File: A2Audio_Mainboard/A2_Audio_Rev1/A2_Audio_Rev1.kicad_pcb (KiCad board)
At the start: 4 copper layers, 30 parts, among them IC1 ES9822QPRO, U1 USBLC6-2SC6, U10 OPA1622IDRCR, U11 SI4732-A10-GS, U12 OPA1612AIDR, U13 LT3042xMSE, U14 W25Q16JVSS, U15 CM5108000, U16 AP2112K-3.3, U17 AP2112K-1.8, U18 LT6711A, U19 TPS62130, U2 TPS65987DDHRSHR, U20 AP2112K-1.8, U21 TPS61230DRC, U22 AP2112K-1.2, U23 LTC2954ITS8-1_TRPBF, U24 TPS65131RGE, U25 LT3094xDD, U26 TS5A3159DBVR, U3 TUSB546A-DCIRNQR, U4 BQ25895RTWR, U5 MAX17055ETB_T, U6 U_DAC_L, U7 U_DAC_R, U8 TPS7A2018PDBVR, U9 TPS7A2033PDBVR

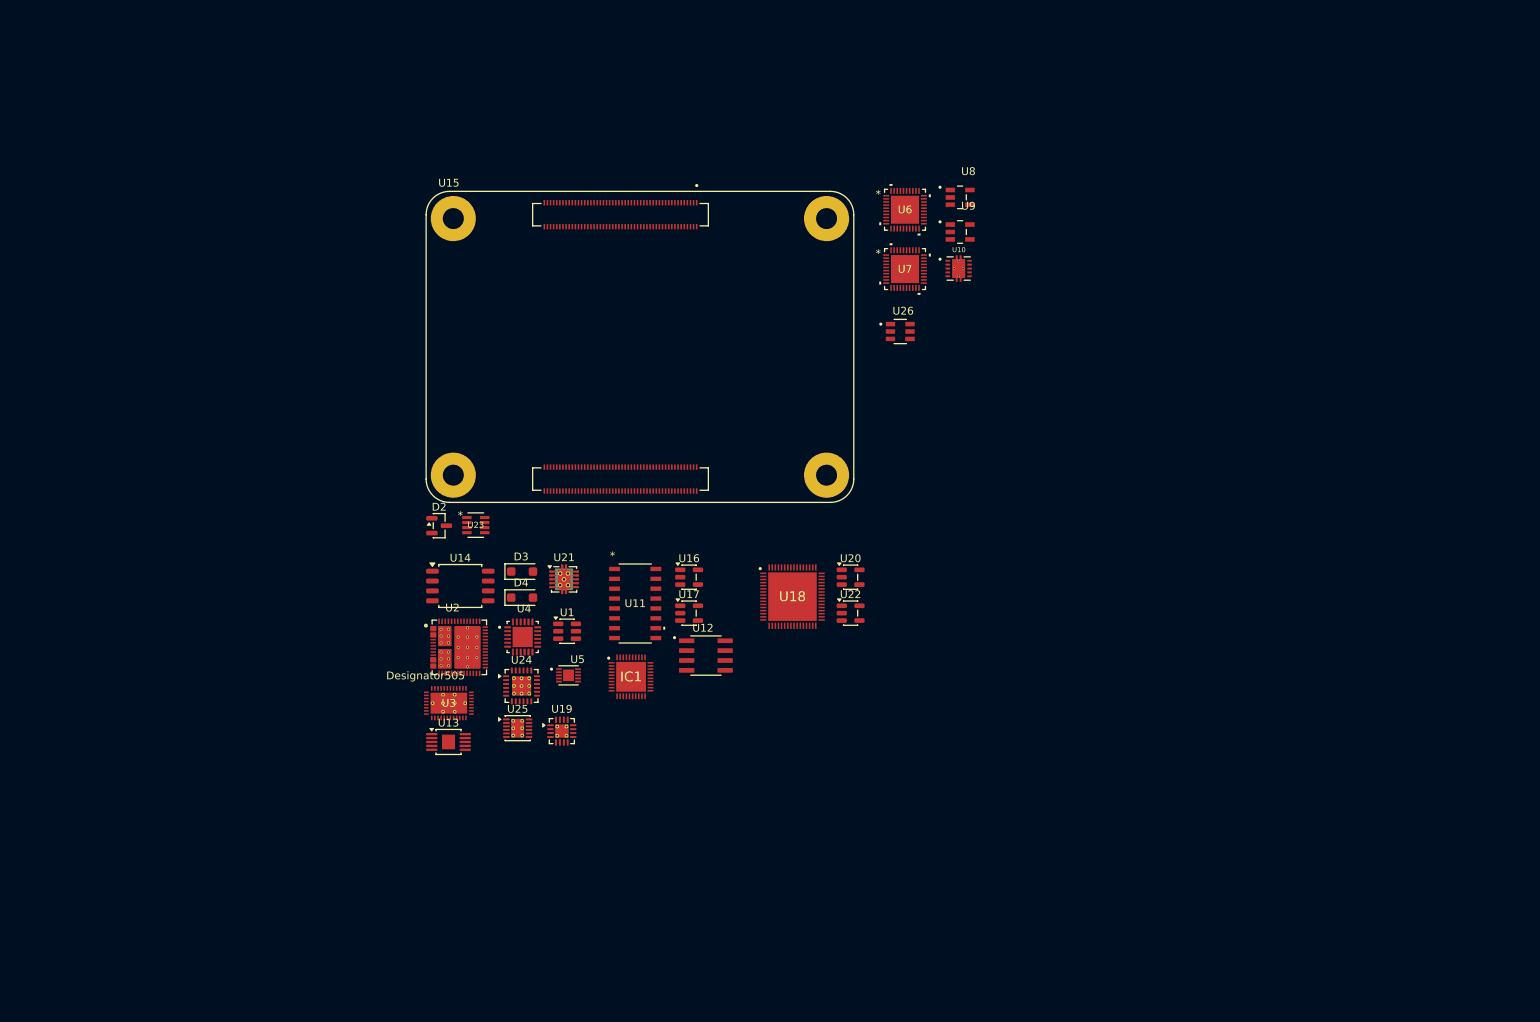
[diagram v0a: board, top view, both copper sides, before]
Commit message: Added footprints and a few more parts.
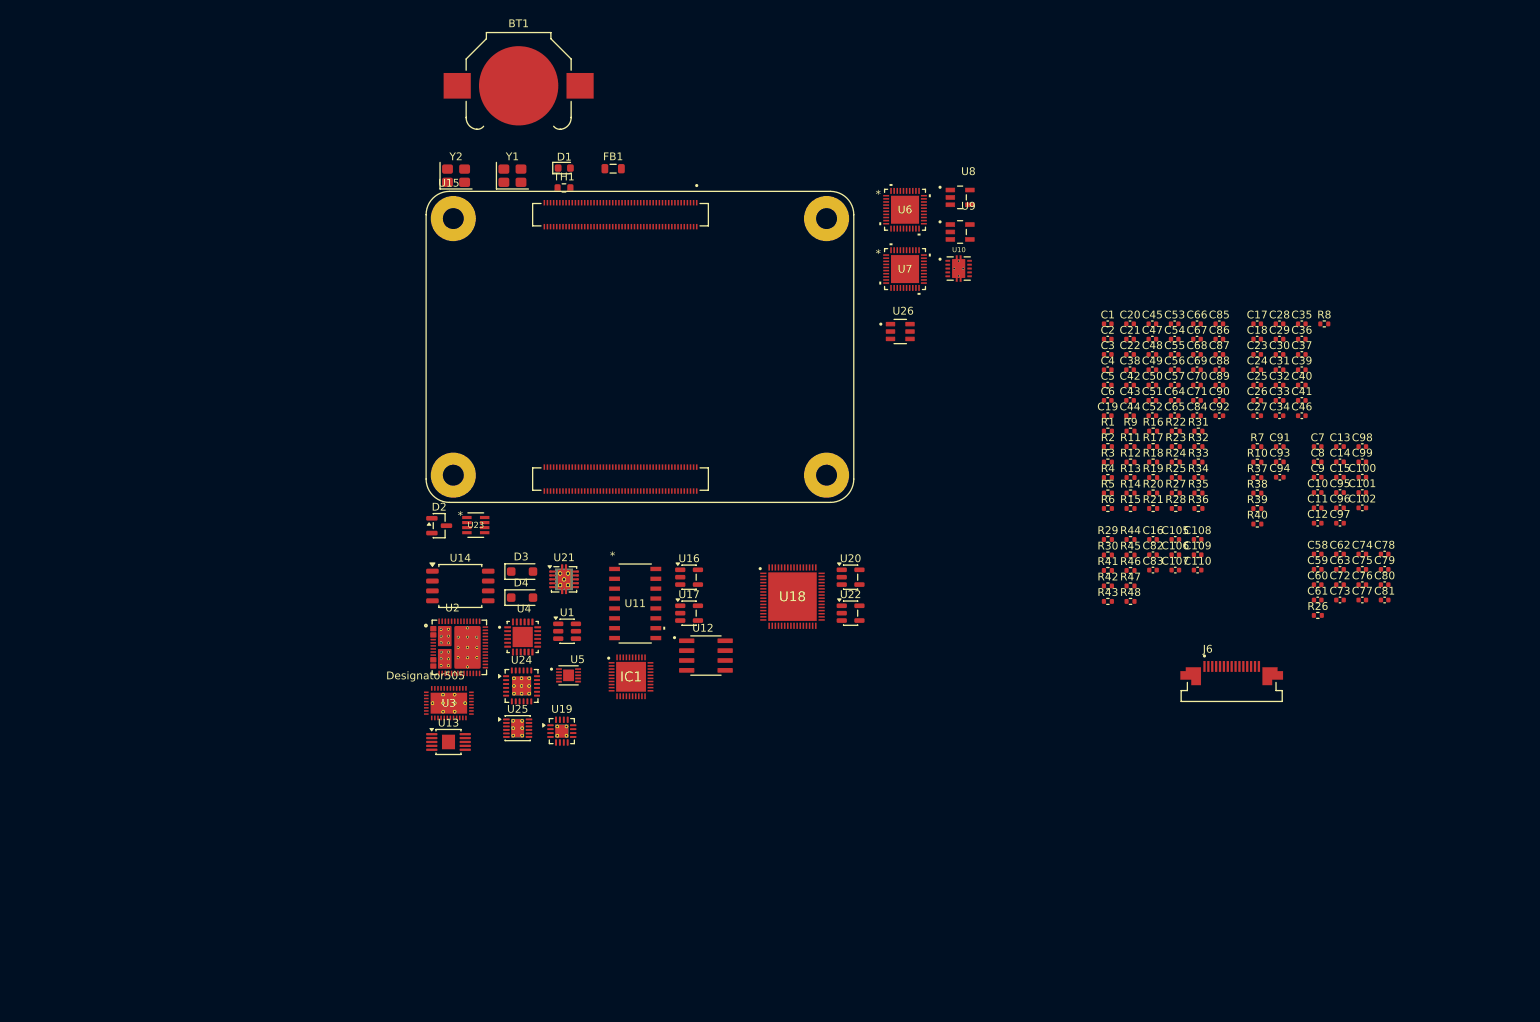
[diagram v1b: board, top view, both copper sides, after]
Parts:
- added BT1: CR1220, Battery:BatteryHolder_Keystone_3000_1x12mm, F.Cu at (116.2, 37.9)
- added C1: 1µF, Capacitor_SMD:C_0402_1005Metric, F.Cu at (191.9, 68.5)
- added C10: 2.2µF, Capacitor_SMD:C_0402_1005Metric, F.Cu at (218.9, 90.2)
- added C100: 1µF, Capacitor_SMD:C_0402_1005Metric, F.Cu at (224.7, 88.2)
- added C101: 2.2µF, Capacitor_SMD:C_0402_1005Metric, F.Cu at (224.7, 90.2)
- added C102: 2.2µF, Capacitor_SMD:C_0402_1005Metric, F.Cu at (224.7, 92.2)
- added C105: 100nF, Capacitor_SMD:C_0402_1005Metric, F.Cu at (200.6, 96.2)
- added C106: 100nF, Capacitor_SMD:C_0402_1005Metric, F.Cu at (200.6, 98.2)
- added C107: 100nF, Capacitor_SMD:C_0402_1005Metric, F.Cu at (200.6, 100.2)
- added C108: 100nF, Capacitor_SMD:C_0402_1005Metric, F.Cu at (203.5, 96.2)
- added C109: 100nF, Capacitor_SMD:C_0402_1005Metric, F.Cu at (203.5, 98.2)
- added C11: 2.2µF, Capacitor_SMD:C_0402_1005Metric, F.Cu at (218.9, 92.2)
- added C110: 100nF, Capacitor_SMD:C_0402_1005Metric, F.Cu at (203.5, 100.2)
- added C12: 2.2µF, Capacitor_SMD:C_0402_1005Metric, F.Cu at (218.9, 94.1)
- added C13: 2.2µF, Capacitor_SMD:C_0402_1005Metric, F.Cu at (221.8, 84.3)
- added C14: 10µF, Capacitor_SMD:C_0402_1005Metric, F.Cu at (221.8, 86.2)
- added C15: 10µF, Capacitor_SMD:C_0402_1005Metric, F.Cu at (221.8, 88.2)
- added C16: 33pF, Capacitor_SMD:C_0402_1005Metric, F.Cu at (197.8, 96.2)
- added C17: 0.1µF, Capacitor_SMD:C_0402_1005Metric, F.Cu at (211.2, 68.5)
- added C18: 0.1µF, Capacitor_SMD:C_0402_1005Metric, F.Cu at (211.2, 70.5)
- added C19: 0.47µF, Capacitor_SMD:C_0402_1005Metric, F.Cu at (191.9, 80.3)
- added C2: 22µF, Capacitor_SMD:C_0402_1005Metric, F.Cu at (191.9, 70.5)
- added C20: 4.7µF, Capacitor_SMD:C_0402_1005Metric, F.Cu at (194.8, 68.5)
- added C21: 4.7µF, Capacitor_SMD:C_0402_1005Metric, F.Cu at (194.8, 70.5)
- added C22: 4.7µF, Capacitor_SMD:C_0402_1005Metric, F.Cu at (194.8, 72.4)
- added C23: 0.1µF, Capacitor_SMD:C_0402_1005Metric, F.Cu at (211.2, 72.4)
- added C24: 2.2µF, Capacitor_SMD:C_0402_1005Metric, F.Cu at (211.2, 74.4)
- added C25: 2.2µF, Capacitor_SMD:C_0402_1005Metric, F.Cu at (211.2, 76.4)
- added C26: 0.1µF, Capacitor_SMD:C_0402_1005Metric, F.Cu at (211.2, 78.3)
- added C27: 10µF, Capacitor_SMD:C_0402_1005Metric, F.Cu at (211.2, 80.3)
- added C28: 0.1µF, Capacitor_SMD:C_0402_1005Metric, F.Cu at (214.0, 68.5)
- added C29: 0.1µF, Capacitor_SMD:C_0402_1005Metric, F.Cu at (214.0, 70.5)
- added C3: 22µF, Capacitor_SMD:C_0402_1005Metric, F.Cu at (191.9, 72.4)
- added C30: 0.1µF, Capacitor_SMD:C_0402_1005Metric, F.Cu at (214.0, 72.4)
- added C31: 0.1µF, Capacitor_SMD:C_0402_1005Metric, F.Cu at (214.0, 74.4)
- added C32: 10µF, Capacitor_SMD:C_0402_1005Metric, F.Cu at (214.0, 76.4)
- added C33: 10µF, Capacitor_SMD:C_0402_1005Metric, F.Cu at (214.0, 78.3)
- added C34: 2.2µF, Capacitor_SMD:C_0402_1005Metric, F.Cu at (214.0, 80.3)
- added C35: 2.2µF, Capacitor_SMD:C_0402_1005Metric, F.Cu at (216.9, 68.5)
- added C36: 2.2µF, Capacitor_SMD:C_0402_1005Metric, F.Cu at (216.9, 70.5)
- added C37: 2.2µF, Capacitor_SMD:C_0402_1005Metric, F.Cu at (216.9, 72.4)
- added C38: 0.1µF, Capacitor_SMD:C_0402_1005Metric, F.Cu at (194.8, 74.4)
- added C39: 1µF, Capacitor_SMD:C_0402_1005Metric, F.Cu at (216.9, 74.4)
- added C4: 10µF, Capacitor_SMD:C_0402_1005Metric, F.Cu at (191.9, 74.4)
- added C40: 1µF, Capacitor_SMD:C_0402_1005Metric, F.Cu at (216.9, 76.4)
- added C41: 1µF, Capacitor_SMD:C_0402_1005Metric, F.Cu at (216.9, 78.3)
- added C42: 0.1µF, Capacitor_SMD:C_0402_1005Metric, F.Cu at (194.8, 76.4)
- added C43: 0.1µF, Capacitor_SMD:C_0402_1005Metric, F.Cu at (194.8, 78.3)
- added C44: 0.1µF, Capacitor_SMD:C_0402_1005Metric, F.Cu at (194.8, 80.3)
- added C45: 0.1µF, Capacitor_SMD:C_0402_1005Metric, F.Cu at (197.7, 68.5)
- added C46: 1µF, Capacitor_SMD:C_0402_1005Metric, F.Cu at (216.9, 80.3)
- added C47: 22µF, Capacitor_SMD:C_0402_1005Metric, F.Cu at (197.7, 70.5)
- added C48: 22µF, Capacitor_SMD:C_0402_1005Metric, F.Cu at (197.7, 72.4)
- added C49: 3.3nF, Capacitor_SMD:C_0402_1005Metric, F.Cu at (197.7, 74.4)
- added C5: 4.7µF, Capacitor_SMD:C_0402_1005Metric, F.Cu at (191.9, 76.4)
- added C50: 100nF, Capacitor_SMD:C_0402_1005Metric, F.Cu at (197.7, 76.4)
- added C51: 100nF, Capacitor_SMD:C_0402_1005Metric, F.Cu at (197.7, 78.3)
- added C52: 100nF, Capacitor_SMD:C_0402_1005Metric, F.Cu at (197.7, 80.3)
- added C53: 2.2µF, Capacitor_SMD:C_0402_1005Metric, F.Cu at (200.5, 68.5)
- added C54: 10nF, Capacitor_SMD:C_0402_1005Metric, F.Cu at (200.5, 70.5)
- added C55: 22µF, Capacitor_SMD:C_0402_1005Metric, F.Cu at (200.5, 72.4)
- added C56: 0.1µF, Capacitor_SMD:C_0402_1005Metric, F.Cu at (200.5, 74.4)
- added C57: 22µF, Capacitor_SMD:C_0402_1005Metric, F.Cu at (200.5, 76.4)
- added C58: 1μF, Capacitor_SMD:C_0402_1005Metric, F.Cu at (218.9, 98.1)
- added C59: 1μF, Capacitor_SMD:C_0402_1005Metric, F.Cu at (218.9, 100.1)
- added C6: 47nF, Capacitor_SMD:C_0402_1005Metric, F.Cu at (191.9, 78.3)
- added C60: 1μF, Capacitor_SMD:C_0402_1005Metric, F.Cu at (218.9, 102.0)
- added C61: 1μF, Capacitor_SMD:C_0402_1005Metric, F.Cu at (218.9, 104.0)
- added C62: 22pF, Capacitor_SMD:C_0402_1005Metric, F.Cu at (221.8, 98.1)
- added C63: 22pF, Capacitor_SMD:C_0402_1005Metric, F.Cu at (221.8, 100.1)
- added C64: 100nF, Capacitor_SMD:C_0402_1005Metric, F.Cu at (200.5, 78.3)
- added C65: 100nF, Capacitor_SMD:C_0402_1005Metric, F.Cu at (200.5, 80.3)
- added C66: 100nF, Capacitor_SMD:C_0402_1005Metric, F.Cu at (203.4, 68.5)
- added C67: 100nF, Capacitor_SMD:C_0402_1005Metric, F.Cu at (203.4, 70.5)
- added C68: 100nF, Capacitor_SMD:C_0402_1005Metric, F.Cu at (203.4, 72.4)
- added C69: 100nF, Capacitor_SMD:C_0402_1005Metric, F.Cu at (203.4, 74.4)
- added C7: 1µF, Capacitor_SMD:C_0402_1005Metric, F.Cu at (218.9, 84.3)
- added C70: 100nF, Capacitor_SMD:C_0402_1005Metric, F.Cu at (203.4, 76.4)
- added C71: 100nF, Capacitor_SMD:C_0402_1005Metric, F.Cu at (203.4, 78.3)
- added C72: 100nF, Capacitor_SMD:C_0402_1005Metric, F.Cu at (221.8, 102.0)
- added C73: 100nF, Capacitor_SMD:C_0402_1005Metric, F.Cu at (221.8, 104.0)
- added C74: 100nF, Capacitor_SMD:C_0402_1005Metric, F.Cu at (224.7, 98.1)
- added C75: 100nF, Capacitor_SMD:C_0402_1005Metric, F.Cu at (224.7, 100.1)
- added C76: 100nF, Capacitor_SMD:C_0402_1005Metric, F.Cu at (224.7, 102.0)
- added C77: 100nF, Capacitor_SMD:C_0402_1005Metric, F.Cu at (224.7, 104.0)
- added C78: 100nF, Capacitor_SMD:C_0402_1005Metric, F.Cu at (227.5, 98.1)
- added C79: 100nF, Capacitor_SMD:C_0402_1005Metric, F.Cu at (227.5, 100.1)
- added C8: 1µF, Capacitor_SMD:C_0402_1005Metric, F.Cu at (218.9, 86.2)
- added C80: 100nF, Capacitor_SMD:C_0402_1005Metric, F.Cu at (227.5, 102.0)
- added C81: 100nF, Capacitor_SMD:C_0402_1005Metric, F.Cu at (227.5, 104.0)
- added C82: 0.33µF, Capacitor_SMD:C_0402_1005Metric, F.Cu at (197.8, 98.2)
- added C83: 0.1µF, Capacitor_SMD:C_0402_1005Metric, F.Cu at (197.8, 100.2)
- added C84: 22µF, Capacitor_SMD:C_0402_1005Metric, F.Cu at (203.4, 80.3)
- added C85: 22µF, Capacitor_SMD:C_0402_1005Metric, F.Cu at (206.3, 68.5)
- added C86: 0.22µF, Capacitor_SMD:C_0402_1005Metric, F.Cu at (206.3, 70.5)
- added C87: 4.7nF, Capacitor_SMD:C_0402_1005Metric, F.Cu at (206.3, 72.4)
- added C88: 4.7nF, Capacitor_SMD:C_0402_1005Metric, F.Cu at (206.3, 74.4)
- added C89: 4.7µF, Capacitor_SMD:C_0402_1005Metric, F.Cu at (206.3, 76.4)
- added C9: 1µF, Capacitor_SMD:C_0402_1005Metric, F.Cu at (218.9, 88.2)
- added C90: 4.7µF, Capacitor_SMD:C_0402_1005Metric, F.Cu at (206.3, 78.3)
- added C91: 10µF, Capacitor_SMD:C_0402_1005Metric, F.Cu at (214.1, 84.3)
- added C92: 4.7µF, Capacitor_SMD:C_0402_1005Metric, F.Cu at (206.3, 80.3)
- added C93: 100nF, Capacitor_SMD:C_0402_1005Metric, F.Cu at (214.1, 86.2)
- added C94: 10µF, Capacitor_SMD:C_0402_1005Metric, F.Cu at (214.1, 88.2)
- added C95: 2.2µF, Capacitor_SMD:C_0402_1005Metric, F.Cu at (221.8, 90.2)
- added C96: 1µF, Capacitor_SMD:C_0402_1005Metric, F.Cu at (221.8, 92.2)
- added C97: 1µF, Capacitor_SMD:C_0402_1005Metric, F.Cu at (221.8, 94.1)
- added C98: 2.2µF, Capacitor_SMD:C_0402_1005Metric, F.Cu at (224.7, 84.3)
- added C99: 1µF, Capacitor_SMD:C_0402_1005Metric, F.Cu at (224.7, 86.2)
- added D1: LED, LED_SMD:LED_0603_1608Metric, F.Cu at (122.0, 48.5)
- added FB1: 600 Ohms @ 100MHz, Inductor_SMD:L_0805_2012Metric, F.Cu at (128.3, 48.5)
- added J6: SFV15R-1STE1HLF, custom:AMPHENOL_SFV15R-1STE1HLF, F.Cu at (207.9, 115.0)
- added R1: 4.7k, Resistor_SMD:R_0402_1005Metric, F.Cu at (192.0, 82.3)
- added R10: 10kΩ, Resistor_SMD:R_0402_1005Metric, F.Cu at (211.2, 86.3)
- added R11: 4.42 kΩ, Resistor_SMD:R_0402_1005Metric, F.Cu at (194.9, 84.3)
- added R12: 23.7 kΩ, Resistor_SMD:R_0402_1005Metric, F.Cu at (194.9, 86.3)
- added R13: 10kΩ, Resistor_SMD:R_0402_1005Metric, F.Cu at (194.9, 88.3)
- added R14: 100kΩ, Resistor_SMD:R_0402_1005Metric, F.Cu at (194.9, 90.2)
- added R15: 32.4kΩ, Resistor_SMD:R_0402_1005Metric, F.Cu at (194.9, 92.2)
- added R16: 100kΩ, Resistor_SMD:R_0402_1005Metric, F.Cu at (197.8, 82.3)
- added R17: 100kΩ, Resistor_SMD:R_0402_1005Metric, F.Cu at (197.8, 84.3)
- added R18: 100kΩ, Resistor_SMD:R_0402_1005Metric, F.Cu at (197.8, 86.3)
- added R19: 100kΩ, Resistor_SMD:R_0402_1005Metric, F.Cu at (197.8, 88.3)
- added R2: 4.7k, Resistor_SMD:R_0402_1005Metric, F.Cu at (192.0, 84.3)
- added R20: 100kΩ, Resistor_SMD:R_0402_1005Metric, F.Cu at (197.8, 90.2)
- added R21: 10kΩ, Resistor_SMD:R_0402_1005Metric, F.Cu at (197.8, 92.2)
- added R22: 10kΩ, Resistor_SMD:R_0402_1005Metric, F.Cu at (200.7, 82.3)
- added R23: 10kΩ, Resistor_SMD:R_0402_1005Metric, F.Cu at (200.7, 84.3)
- added R24: 130Ω, Resistor_SMD:R_0402_1005Metric, F.Cu at (200.7, 86.3)
- added R25: 10kΩ, Resistor_SMD:R_0402_1005Metric, F.Cu at (200.7, 88.3)
- added R26: 2kΩ, Resistor_SMD:R_0402_1005Metric, F.Cu at (219.0, 106.0)
- added R27: 100kΩ, Resistor_SMD:R_0402_1005Metric, F.Cu at (200.7, 90.2)
- added R28: 316kΩ, Resistor_SMD:R_0402_1005Metric, F.Cu at (200.7, 92.2)
- added R29: 10k, Resistor_SMD:R_0402_1005Metric, F.Cu at (192.0, 96.2)
- added R3: 10mΩ, Resistor_SMD:R_0402_1005Metric, F.Cu at (192.0, 86.3)
- added R30: 100k, Resistor_SMD:R_0402_1005Metric, F.Cu at (192.0, 98.2)
- added R31: 1MΩ, Resistor_SMD:R_0402_1005Metric, F.Cu at (203.6, 82.3)
- added R32: 255kΩ, Resistor_SMD:R_0402_1005Metric, F.Cu at (203.6, 84.3)
- added R33: 205kΩ, Resistor_SMD:R_0402_1005Metric, F.Cu at (203.6, 86.3)
- added R34: 205kΩ, Resistor_SMD:R_0402_1005Metric, F.Cu at (203.6, 88.3)
- added R35: 100kΩ, Resistor_SMD:R_0402_1005Metric, F.Cu at (203.6, 90.2)
- added R36: 100kΩ, Resistor_SMD:R_0402_1005Metric, F.Cu at (203.6, 92.2)
- added R37: 10kΩ, Resistor_SMD:R_0402_1005Metric, F.Cu at (211.2, 88.3)
- added R38: 10kΩ, Resistor_SMD:R_0402_1005Metric, F.Cu at (211.2, 90.3)
- added R39: 10kΩ, Resistor_SMD:R_0402_1005Metric, F.Cu at (211.2, 92.2)
- added R4: 49.9kΩ, Resistor_SMD:R_0402_1005Metric, F.Cu at (192.0, 88.3)
- added R40: 100kΩ, Resistor_SMD:R_0402_1005Metric, F.Cu at (211.2, 94.2)
- added R41: 10kΩ, Resistor_SMD:R_0402_1005Metric, F.Cu at (192.0, 100.2)
- added R42: 10kΩ, Resistor_SMD:R_0402_1005Metric, F.Cu at (192.0, 102.2)
- added R43: 10kΩ, Resistor_SMD:R_0402_1005Metric, F.Cu at (192.0, 104.2)
- added R44: 10kΩ, Resistor_SMD:R_0402_1005Metric, F.Cu at (194.9, 96.2)
- added R45: 10kΩ, Resistor_SMD:R_0402_1005Metric, F.Cu at (194.9, 98.2)
- added R46: 10kΩ, Resistor_SMD:R_0402_1005Metric, F.Cu at (194.9, 100.2)
- added R47: 10kΩ, Resistor_SMD:R_0402_1005Metric, F.Cu at (194.9, 102.2)
- added R48: 10kΩ, Resistor_SMD:R_0402_1005Metric, F.Cu at (194.9, 104.2)
- added R5: 49.9kΩ, Resistor_SMD:R_0402_1005Metric, F.Cu at (192.0, 90.2)
- added R6: 10kΩ, Resistor_SMD:R_0402_1005Metric, F.Cu at (192.0, 92.2)
- added R7: 10kΩ, Resistor_SMD:R_0402_1005Metric, F.Cu at (211.2, 84.3)
- added R8: 10kΩ, Resistor_SMD:R_0402_1005Metric, F.Cu at (219.8, 68.5)
- added R9: R, Resistor_SMD:R_0402_1005Metric, F.Cu at (194.9, 82.3)
- added TH1: 10kΩ NTC, Resistor_SMD:R_0603_1608Metric, F.Cu at (122.0, 51.0)
- added Y1: Crystal, Crystal:Crystal_SMD_3225-4Pin_3.2x2.5mm, F.Cu at (115.4, 49.4)
- added Y2: 27MHz, Crystal:Crystal_SMD_3225-4Pin_3.2x2.5mm, F.Cu at (108.1, 49.4)

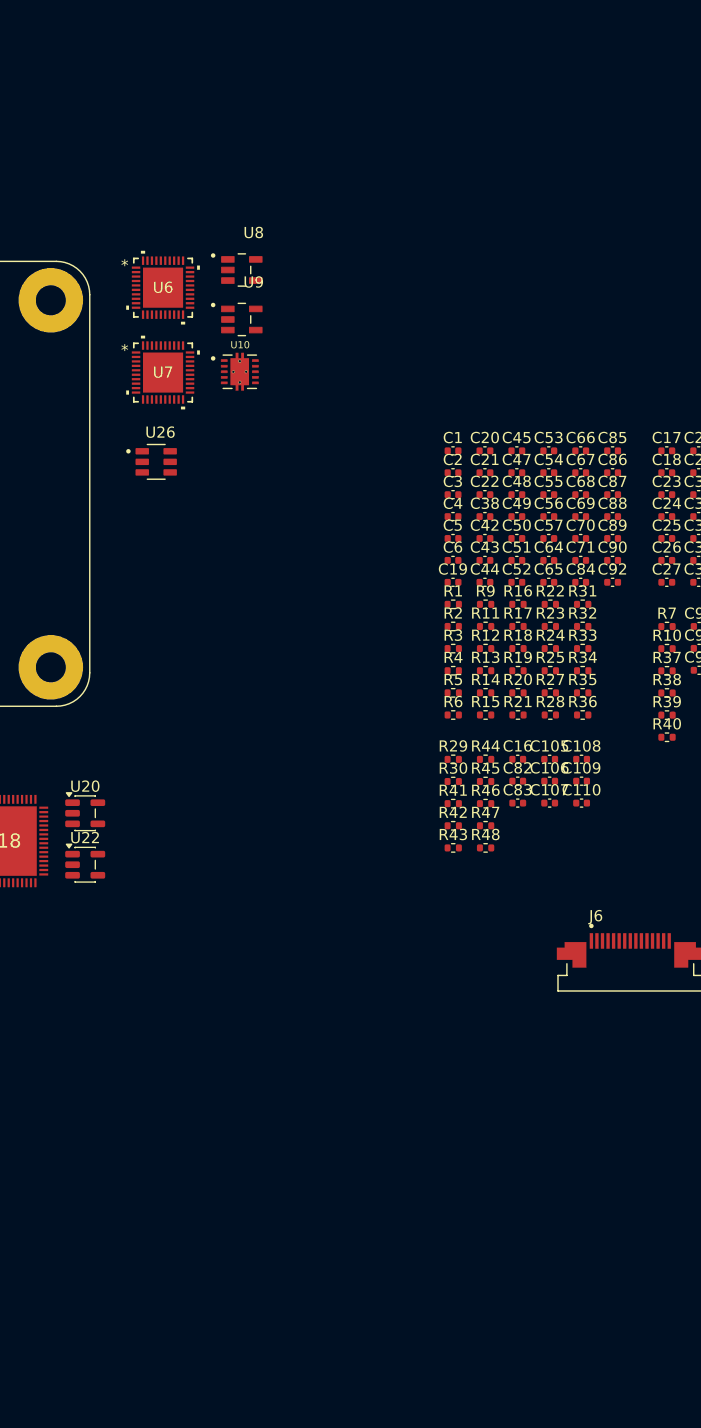
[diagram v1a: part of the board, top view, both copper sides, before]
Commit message: Refining of logic and adding battery connector
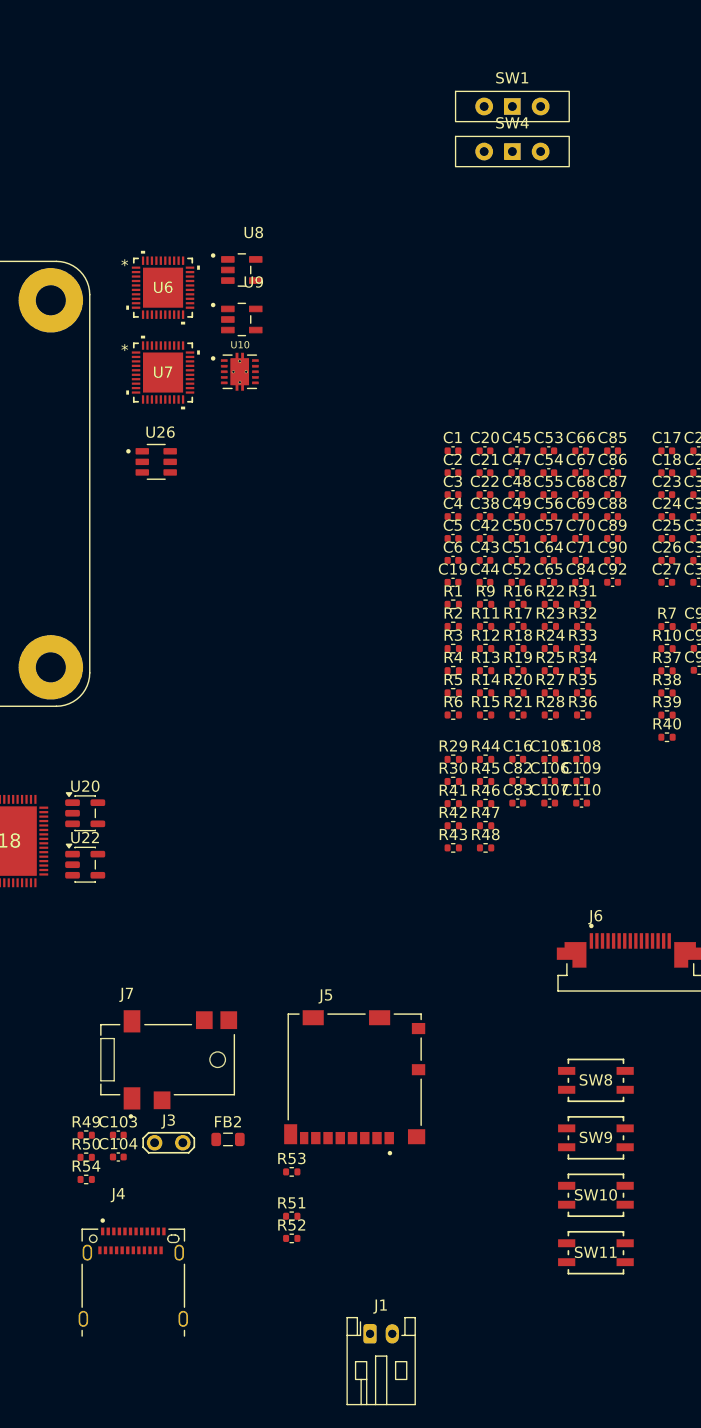
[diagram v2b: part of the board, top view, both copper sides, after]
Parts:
- added C103: 1µF, Capacitor_SMD:C_0402_1005Metric, F.Cu at (161.8, 130.0)
- added C104: 100pF, Capacitor_SMD:C_0402_1005Metric, F.Cu at (161.8, 132.0)
- added FB2: FerriteBead, Inductor_SMD:L_0805_2012Metric, F.Cu at (171.7, 130.4)
- added J1: Battery_Connector, Connector_JST:JST_PH_S2B-PH-K_1x02_P2.00mm_Horizontal, F.Cu at (184.5, 147.9)
- added J3: BOOT_JUMPER, TestPoint:TestPoint_2Pads_Pitch2.54mm_Drill0.8mm, F.Cu at (165.1, 130.7)
- added J4: 12401610E4_2A, custom:AMPHENOL_12401610E4_2A, F.Cu at (163.2, 143.7)
- added J5: 104031-0811, custom:MOLEX_104031-0811, F.Cu at (183.1, 124.8)
- added J7: SJ2-35954B-SMT-TR, custom:CUI_SJ2-35954B-SMT-TR, F.Cu at (166.3, 123.2)
- added R49: 2.2kΩ, Resistor_SMD:R_0402_1005Metric, F.Cu at (159.0, 130.0)
- added R50: 10kΩ, Resistor_SMD:R_0402_1005Metric, F.Cu at (159.0, 132.0)
- added R51: 10kΩ, Resistor_SMD:R_0402_1005Metric, F.Cu at (177.4, 137.3)
- added R52: 10kΩ, Resistor_SMD:R_0402_1005Metric, F.Cu at (177.4, 139.3)
- added R53: 10kΩ, Resistor_SMD:R_0402_1005Metric, F.Cu at (177.4, 133.3)
- added R54: 10kΩ, Resistor_SMD:R_0402_1005Metric, F.Cu at (159.0, 134.0)
- added SW1: SW_Wuerth_450301014042, Button_Switch_THT:SW_Slide-03_Wuerth-WS-SLTV_10x2.5x6.4_P2.54mm, F.Cu at (197.3, 37.5)
- added SW10: EVQ-PUJ02K, custom:SW_EVQPUJ_4P7X3P5_PAN, F.Cu at (204.8, 135.4)
- added SW11: EVQ-PUJ02K, custom:SW_EVQPUJ_4P7X3P5_PAN, F.Cu at (204.8, 140.6)
- added SW4: SW_Wuerth_450301014042, Button_Switch_THT:SW_Slide-03_Wuerth-WS-SLTV_10x2.5x6.4_P2.54mm, F.Cu at (197.3, 41.6)
- added SW8: EVQ-PUJ02K, custom:SW_EVQPUJ_4P7X3P5_PAN, F.Cu at (204.8, 125.1)
- added SW9: EVQ-PUJ02K, custom:SW_EVQPUJ_4P7X3P5_PAN, F.Cu at (204.8, 130.2)
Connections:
- net /Power&Battery/VBUS_RAW renamed VBUS_A
- C24 pad 1: Net-(U12-+IN_A) -> Net-(C24-Pad1)
- C25 pad 2: Net-(U12-+IN_B) -> Net-(C25-Pad2)
- C42 pad 1: Net-(J1-TX1-) -> /Power&Battery/TX1-1
- C43 pad 1: Net-(J1-TX1+) -> /Power&Battery/TX1+1
- C44 pad 1: Net-(J1-TX2-) -> /Power&Battery/TX2-1
- C45 pad 1: Net-(J1-TX2+) -> /Power&Battery/TX2+1
- C9 pad 1: /Audio_Engine/1V8_DIG -> /Audio_Engine/3V3_ANA
- U1 pad 1: Net-(J1-D--PadA7) -> /Power&Battery/D-1
- U1 pad 3: Net-(J1-D+-PadA6) -> /Power&Battery/D+1
- U10 pad 8: /Audio_Engine/1V8_DIG -> /Audio_Engine/3V3_ANA
- U12 pad 3: Net-(U12-+IN_A) -> /MIC_IN
- U15 pad 31: unconnected-(U15A-GPIO12-Pad31) -> /CARD_DETECT
- U15 pad 55: unconnected-(U15A-GPIO14-Pad55) -> /HP_DETECT
- U15 pad 94: /Power&Battery/TYPEC_CC1 -> unconnected-(U15A-CC1-Pad94)
- U15 pad 96: /Power&Battery/TYPEC_CC2 -> unconnected-(U15A-CC2-Pad96)
- U2 pad 24: /Power&Battery/TYPEC_CC1 -> /Power&Battery/CC11
- U2 pad 26: /Power&Battery/TYPEC_CC2 -> /Power&Battery/CC21
- U3 pad 26: Net-(J1-SBU2) -> /Power&Battery/SBU2
- U3 pad 27: Net-(J1-SBU1) -> /Power&Battery/SBU1
- U3 pad 30: /Power&Battery/TYPEC_RX1_P -> /Power&Battery/RX1+1
- U3 pad 31: /Power&Battery/TYPEC_RX1_N -> /Power&Battery/RX1-1
- U3 pad 39: /Power&Battery/TYPEC_RX2_N -> /Power&Battery/RX2-1
- U3 pad 40: /Power&Battery/TYPEC_RX2_P -> /Power&Battery/RX2+1
- U6 pad 25: /Audio_Engine/1V8_DIG -> /Audio_Engine/3V3_ANA
- U6 pad 26: /Audio_Engine/1V8_DIG -> /Audio_Engine/3V3_ANA
- U6 pad 31: /Audio_Engine/1V8_DIG -> /Audio_Engine/3V3_ANA
- U6 pad 7: /Audio_Engine/1V8_DIG -> /Audio_Engine/3V3_ANA
- U7 pad 25: /Audio_Engine/1V8_DIG -> /Audio_Engine/3V3_ANA
- U7 pad 26: /Audio_Engine/1V8_DIG -> /Audio_Engine/3V3_ANA
- U7 pad 30: /Audio_Engine/1V8_DIG -> /Audio_Engine/3V3_ANA
- U7 pad 31: /Audio_Engine/1V8_DIG -> /Audio_Engine/3V3_ANA
- U7 pad 7: /Audio_Engine/1V8_DIG -> /Audio_Engine/3V3_ANA
- U9 pad 5: /Audio_Engine/1V8_DIG -> /Audio_Engine/3V3_ANA
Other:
- board outline added: 1.2 x 3.8 mm
